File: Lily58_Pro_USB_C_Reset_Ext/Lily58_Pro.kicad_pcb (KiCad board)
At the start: 2 copper layers, 7.7 x 47.2 mm, 11 parts, among them J2 4PIN, P1 i2c_pin, U1 USB4110-GF-A_REVB, U2 USB4110-GF-A_REVB

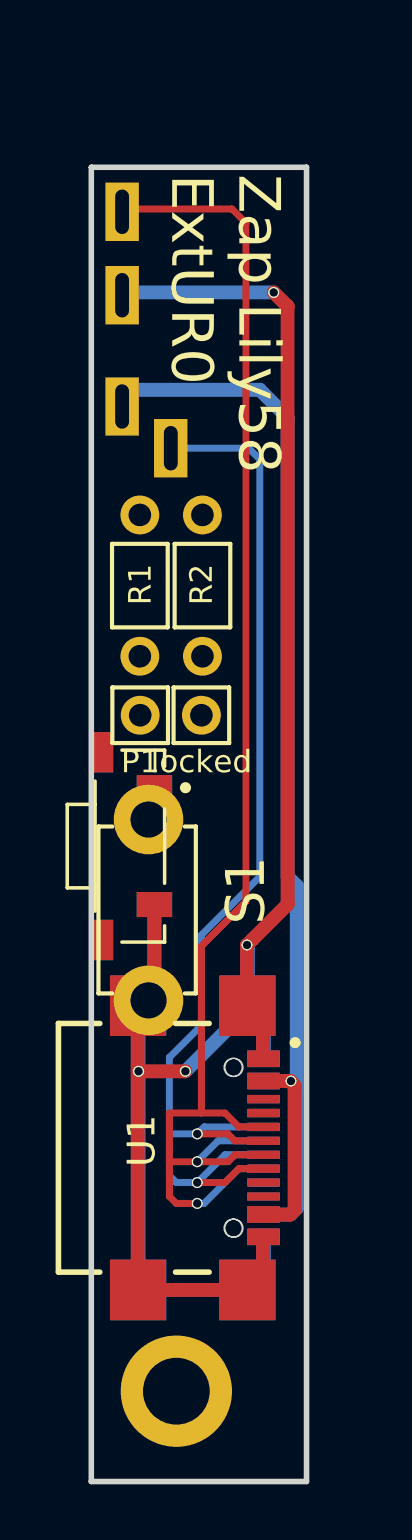
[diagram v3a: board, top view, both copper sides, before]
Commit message: Lily58_Pro_USB_C_Reset_Ext: update via size
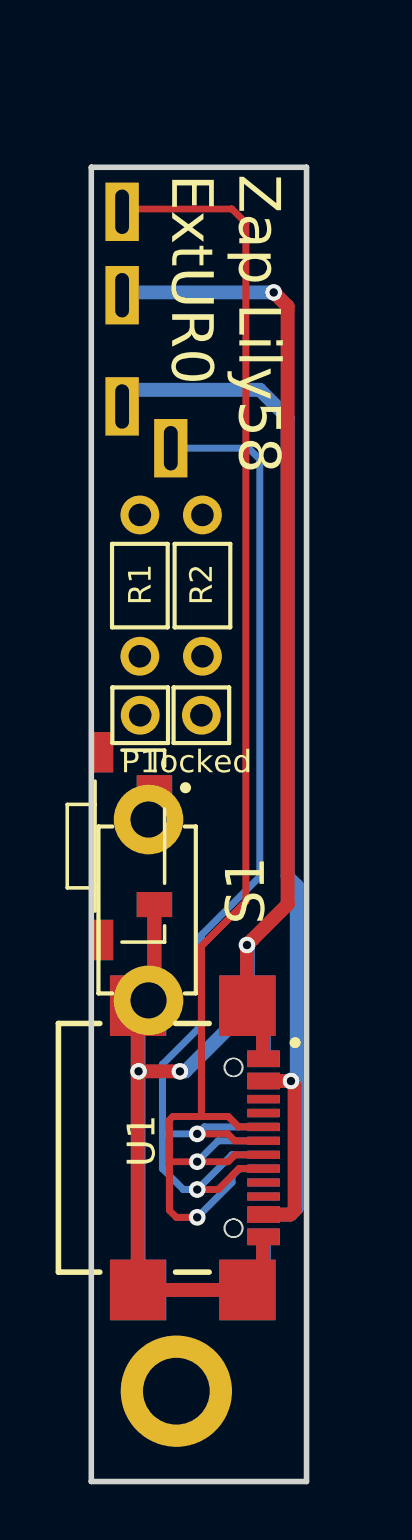
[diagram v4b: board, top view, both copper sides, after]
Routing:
- net SDA: track 42.4 -> 43.2 mm
- net SCL: track 54.1 -> 54.7 mm
